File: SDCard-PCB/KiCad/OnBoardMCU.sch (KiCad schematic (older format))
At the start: 26 parts, among them J6 Conn_01x01, J7 Conn_01x01, J8 Conn_01x08, U2 ATSAME70N21A-CN, U3 TSOP57438TT1, Y1 ABM8G-12.000MHZ-4Y-T3

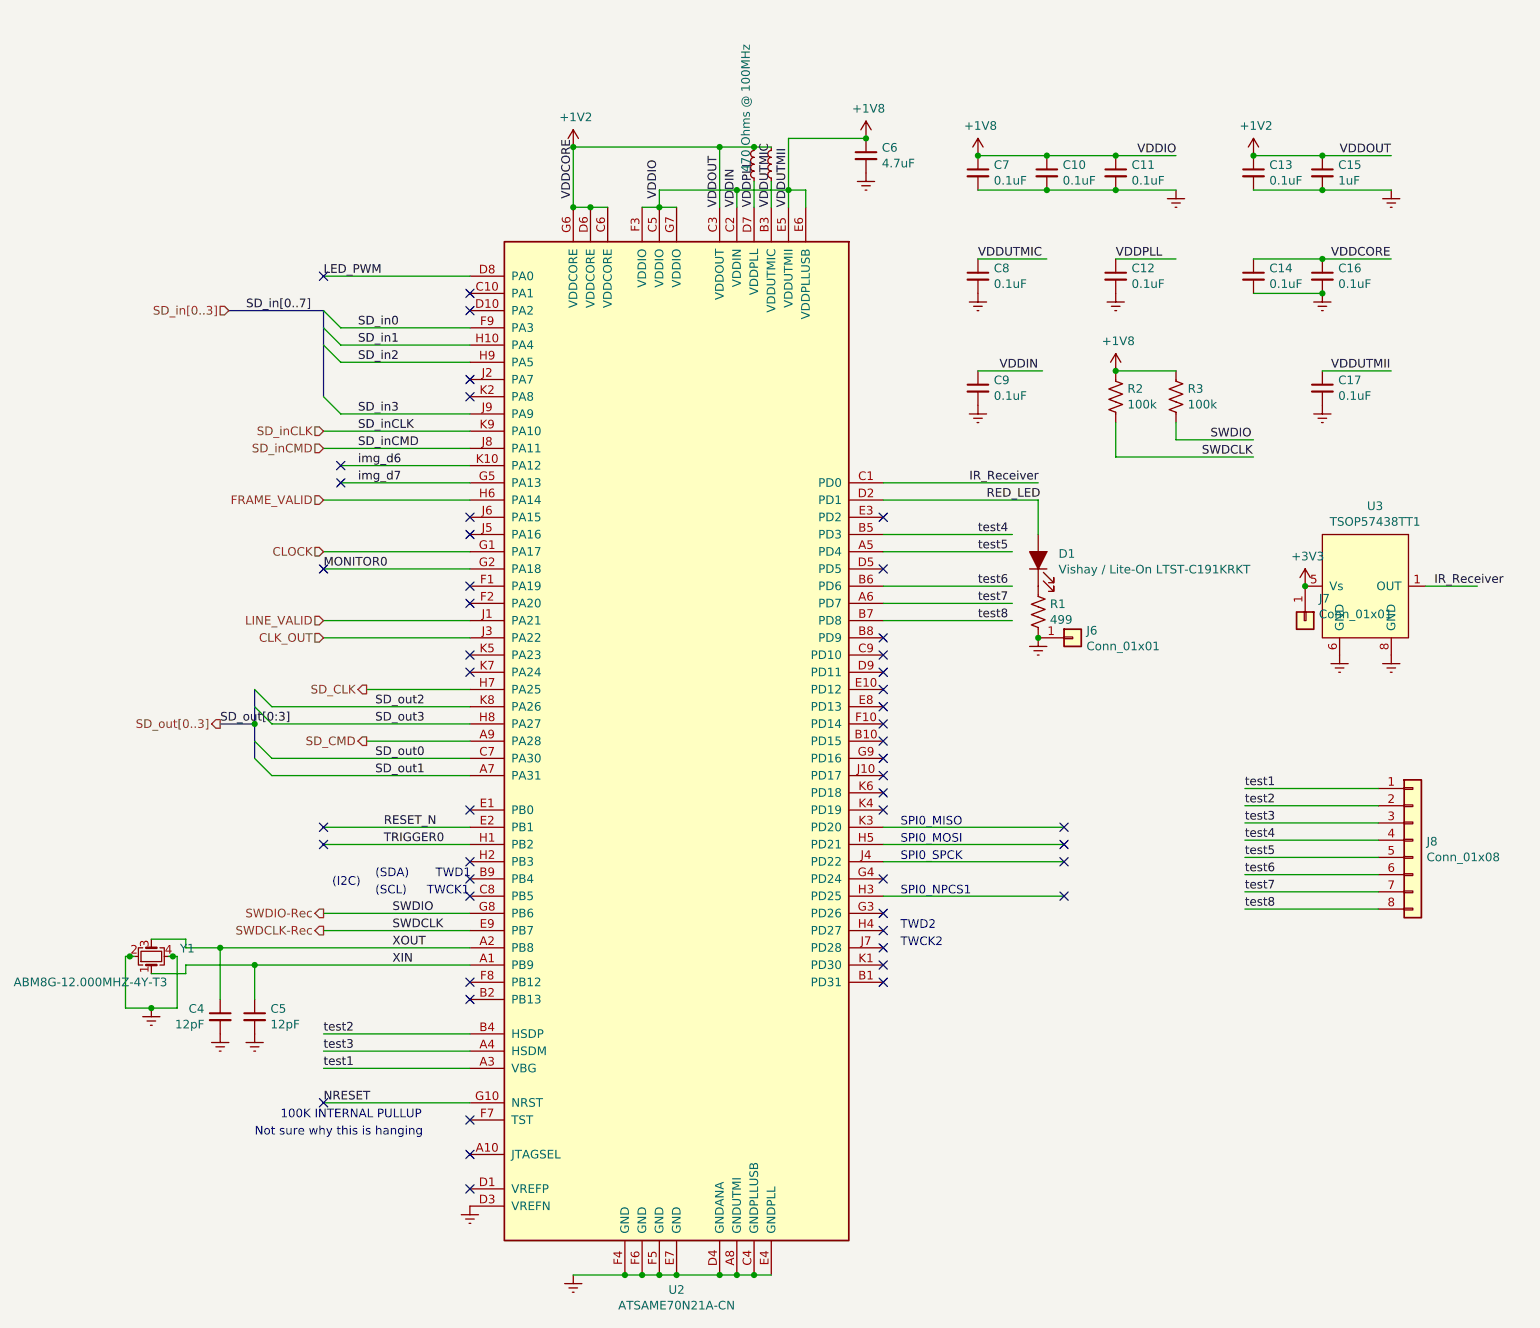
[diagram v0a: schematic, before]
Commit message: Finish schematics, begin PCB design
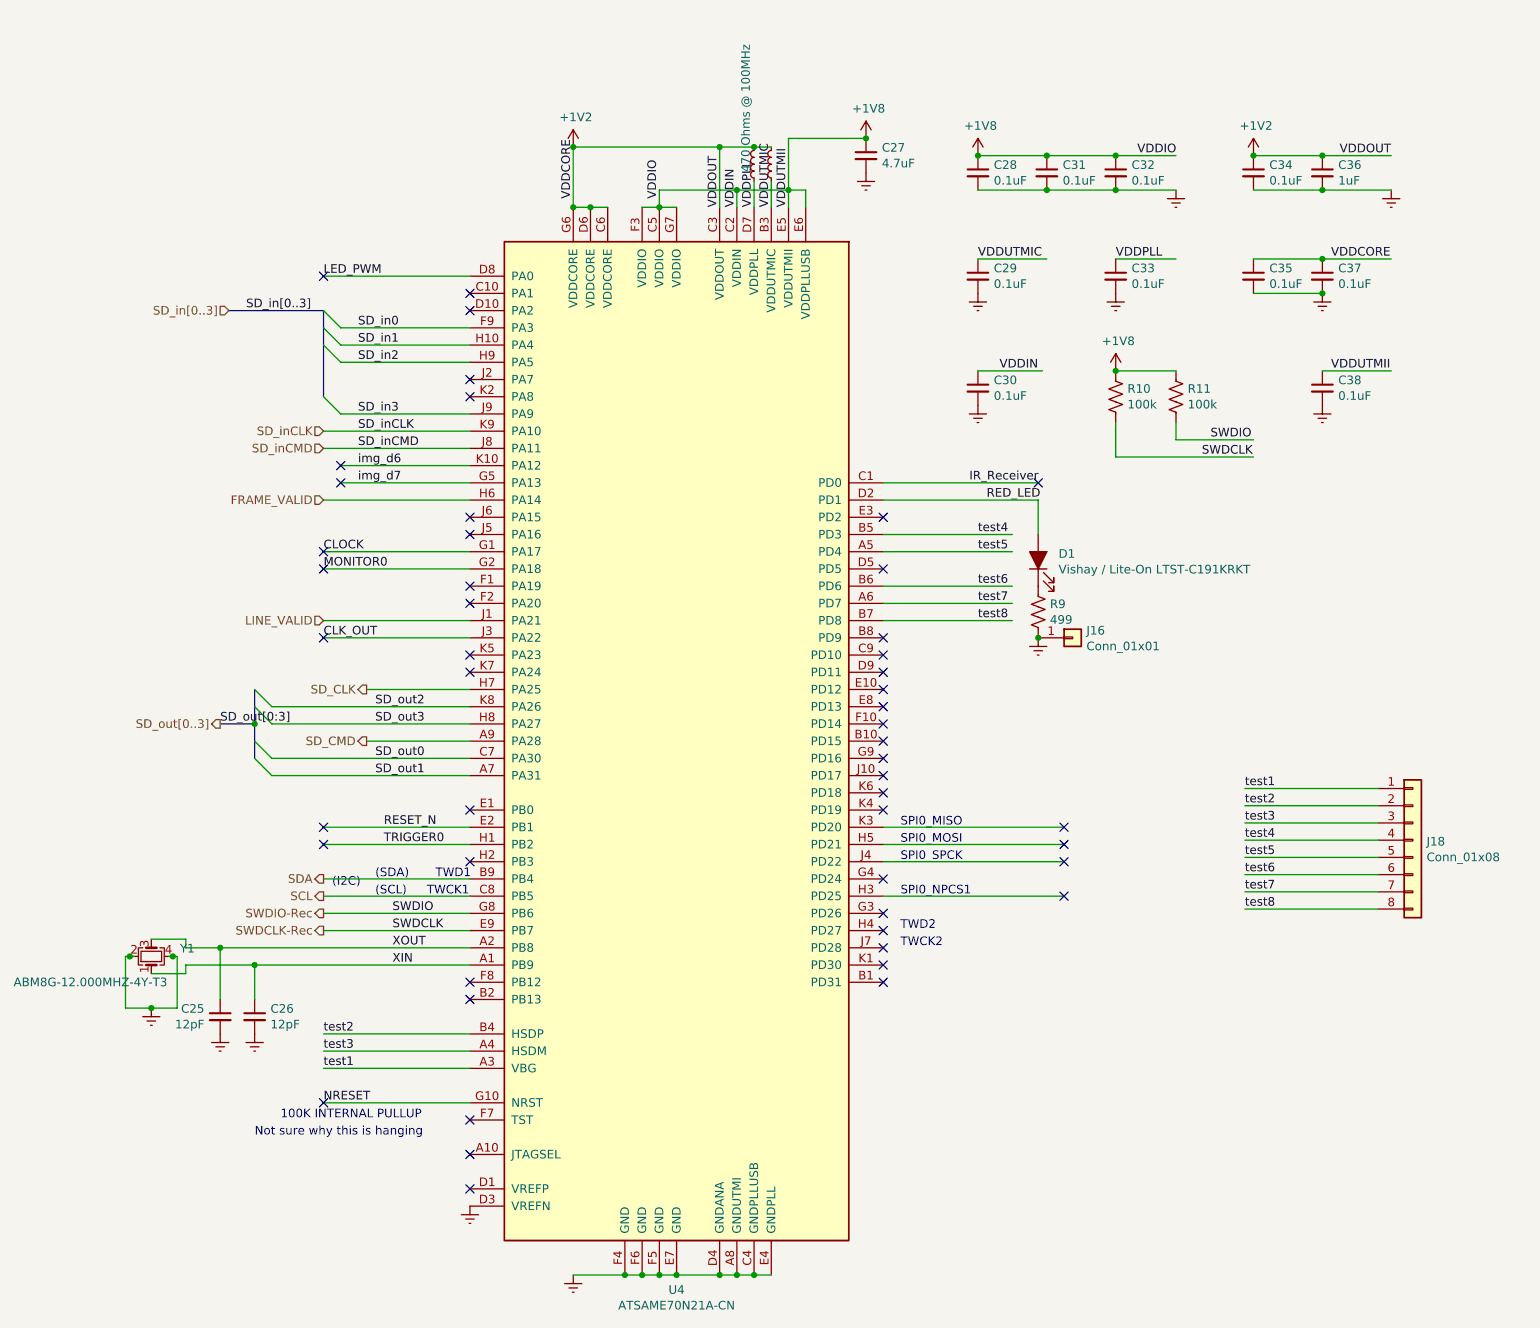
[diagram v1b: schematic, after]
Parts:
- removed J7: Conn_01x01, .Connector:Conn_1x1_700_Circular_Pad, symbol .Connector:Conn_01x01
- removed U3: TSOP57438TT1, .Package_SON:SON_4_P300_395X395X90L55X35L, symbol .IR_Receiver:TSOP57438TT1
- renumbered C4 to C25, C5 to C26, C6 to C27, C7 to C28, C8 to C29, C9 to C30, C10 to C31, C11 to C32, C12 to C33, C13 to C34, C14 to C35, C15 to C36, C16 to C37, C17 to C38, J6 to J16, J8 to J18, L1 to L7, L2 to L8, R2 to R10, R3 to R11, R1 to R9, U2 to U4
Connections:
- net labels added: SCL, SDA
- net labels removed: +3V3, SD_in[0..7]
- wire segments 117 -> 118
- no-connect marks 49 -> 50

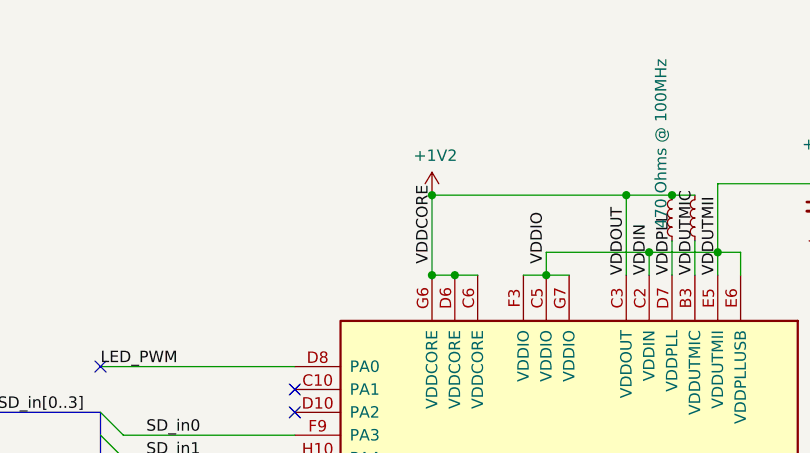
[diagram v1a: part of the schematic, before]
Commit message: PlugIn PCB Ready
1. Completes the PCBNew drawing for MicroSD PlugIn PCB
2. Passes the DRC rule check
3. Generate Gerber files
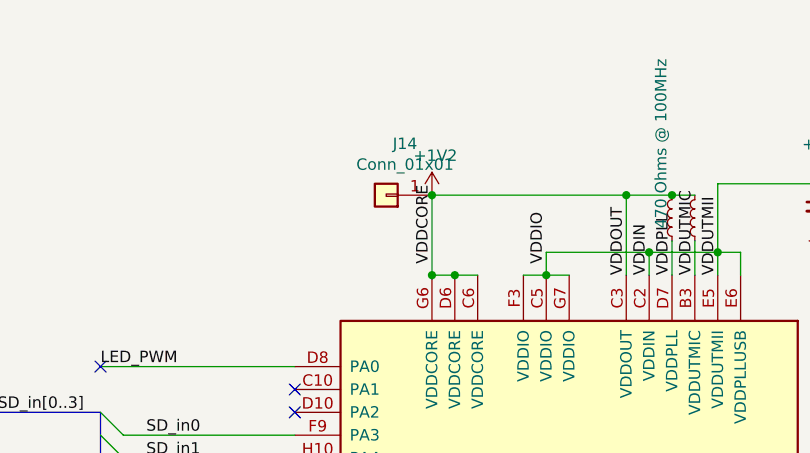
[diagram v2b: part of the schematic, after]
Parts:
- added J14: Conn_01x01, .Connector:Conn_1x1_700_Circular_Pad, symbol .Connector:Conn_01x01
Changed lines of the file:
@@
 Wire Bus Line
 	3500 1650 3500 2150
+$Comp
+L .Connector:Conn_01x01 J14
+U 1 1 5D003D2A
+P 4750 700
+F 0 "J14" H 4668 475 50  0000 C CNN
+F 1 "Conn_01x01" H 4668 566 50  0000 C CNN
+F 2 ".Connector:Conn_1x1_700_Circular_Pad" H 4750 700 50  0001 C CNN
+F 3 "~" H 4750 700 50  0001 C CNN
+	1    4750 700
+	-1   0    0    1
+$EndComp
 $EndSCHEMATC
